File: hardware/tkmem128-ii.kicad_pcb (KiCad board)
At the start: 4 copper layers, 78.7 x 66 mm, 22 parts, among them J1 Barramento TK, U1 GAL20V8B, U2 74HCT273, U3 AS6C1008-55PCN, U4 27C256

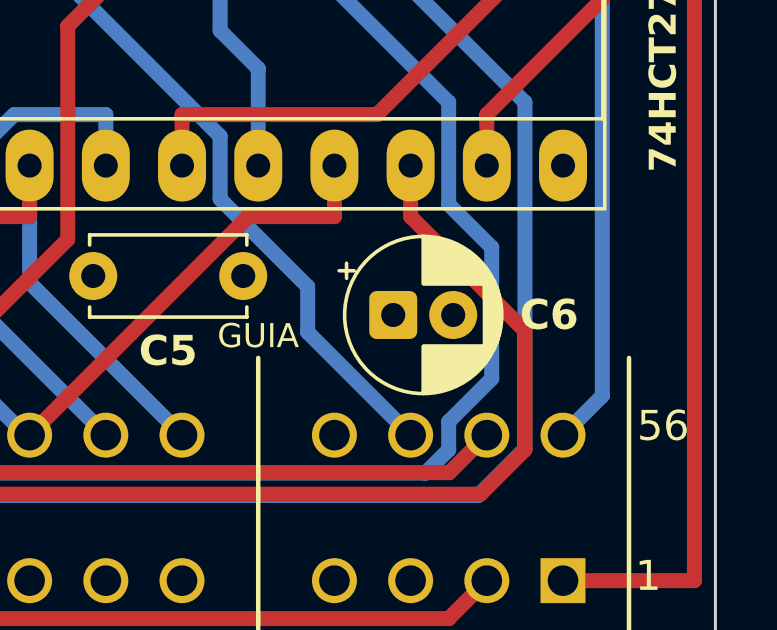
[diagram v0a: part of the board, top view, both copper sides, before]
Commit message: Afasta C6 tambem na horizontal: 0,80 mm para a esquerda
Depois de subir, a ilha 2 de C6 ainda ficava a 0,234 mm de uma vertical de D5
na face de tras. Dentro da regra (0,20), mas era a menor folga da placa
inteira, e num ponto onde a solda de um eletrolitico de 5 mm e feita a mao.

Andar na horizontal ataca essa folga de frente — 1 mm por milimetro, em vez de
1/raiz(2) como a diagonal do D3. Varredura de -0,1 a -2,5 mm:

    -0,10  0,334   (sai de cima do D5)
    -0,80  0,806   <- maximo
    -1,50  0,302
    -1,80  0,002   (a ilha 1 encosta no D7, que vem pelo outro lado)

Existe um otimo e ele nao esta na ponta: passar de 0,80 comeca a piorar. A pior
folga de C6 vai de 0,234 para 0,806 mm — 3,4 vezes — e as duas trilhas que
sobram mais perto (D7 a 0,806 e D3 a 0,831) ficam equilibradas.

O que nao mudou: 1,13 mm ate os terminais de J1 e 1,11 mm ate o corpo do
soquete de U2, porque o deslocamento e so horizontal. Sem rerotear, de novo:
as ilhas de C6 sao +5V e GND e tocam os planos internos direto.

DRC 0/0, os quatro conferidores OK.

Co-Authored-By: Claude Opus 5 <noreply@anthropic.com>
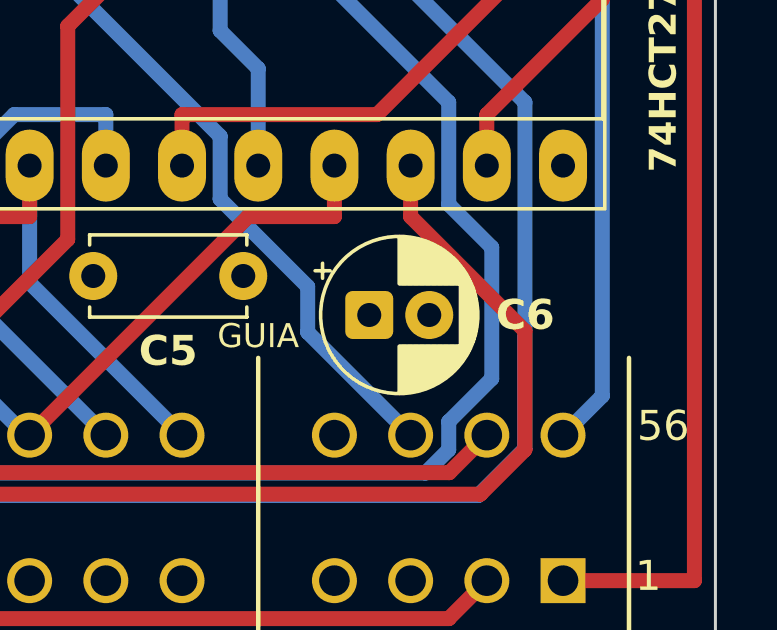
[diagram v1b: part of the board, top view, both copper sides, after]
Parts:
- moved C6 0.80 mm to (67.2, 54.3)
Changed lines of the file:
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@@
 	(footprint "CP_Radial_D5.0mm_P2.00mm"
 		(layer "F.Cu")
-		(at 68 54.3)
+		(at 67.2 54.3)
 		(descr "CP, Radial series, Radial, pin pitch=2.00mm, diameter=5mm, height=7mm, Electrolytic Capacitor")
 		(tags "CP Radial series Radial pin pitch 2.00mm diameter 5mm height 7mm Electrolytic Capacitor")

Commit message: Nota do R4 em duas linhas, e "do TK" vira "do micro"
Era uma linha so de 57 caracteres e 43,4 mm — mais da metade da largura da
placa, atravessando o verso inteiro. Agora sao duas: a funcao em cima, o efeito
entre parenteses embaixo, 28,1 mm na mais larga.

"do TK" virou "do micro" porque o pino 29 e N.C. nas duas maquinas e a placa
serve nas duas. O que e especifico do TK e o PONTO INTERNO onde o fio chega
(pino 10 do IC27), e isso e assunto de docs/PREPARAR-O-TK.md, nao de
serigrafia.

Nota de ferramenta: o mapa de espaco livre acusava a faixa y 49..51 como
ocupada, e o unico ocupante era o proprio texto que eu ia substituir. A
exclusao estava escrita como `d is not t`, e no SWIG dois proxies diferentes
podem embrulhar o mesmo objeto C++ — a identidade Python nao serve para
comparar itens do pcbnew.

DRC 0/0, os quatro conferidores OK.

Co-Authored-By: Claude Opus 5 <noreply@anthropic.com>
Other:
- board text added: "(auto-desativa a RAM de 32K do micro)"
- board text added: "R4: pull-up do pino 29"
- board text removed: "R4: pull-up do pino 29 (auto-desativa a RAM de 32K do TK)"
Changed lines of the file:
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@@
+		)
+	)
+	(gr_text "R4: pull-up do pino 29"
+		(at 23.5 49.4 0)
+		(layer "B.SilkS")
+		(effects
+			(font
+				(size 0.9 0.9)
+				(thickness 0.18)
+			)
+			(justify mirror)
+		)
+	)
+	(gr_text "(auto-desativa a RAM de 32K do micro)"
+		(at 23.5 51.6 0)
+		(layer "B.SilkS")
+		(effects
+			(font
+				(size 0.9 0.9)
+				(thickness 0.18)
+			)
+			(justify mirror)
 		)
 	)
@@
 		(layer "B.SilkS")
 		(effects
-			(font
-				(size 0.9 0.9)
-				(thickness 0.18)
-				(bold yes)
-			)
-			(justify mirror)
-		)
-	)
-	(gr_text "R4: pull-up do pino 29 (auto-desativa a RAM de 32K do TK)"
-		(at 23.5 50.5 0)
-		(layer "B.SilkS")
-		(effects
